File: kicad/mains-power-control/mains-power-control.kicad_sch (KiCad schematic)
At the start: 21 parts, among them J1 Conn_01x02_Socket, J2 Conn_01x03_Socket, J3 Conn_01x03_Pin, J4 Conn_01x06_Pin, J5 Conn_01x04_Pin, J6 Conn_01x02_Pin, U1 BP, U2 SeeeduinoXIAO, U3 MOC3020M, U5 H11AA1

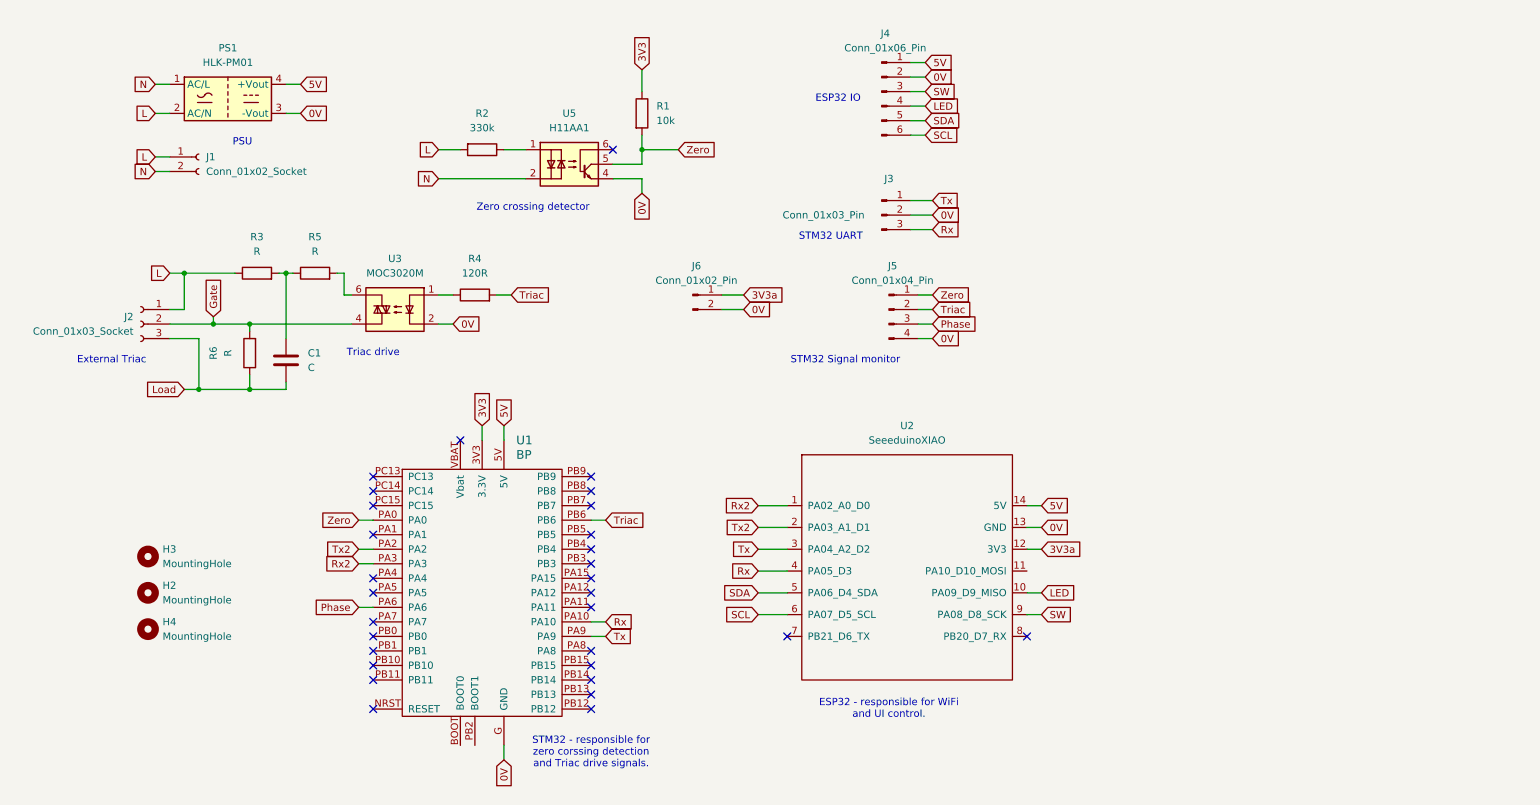
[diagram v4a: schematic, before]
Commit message: wip: adding fan driver and onewire to v 1.1 pcb
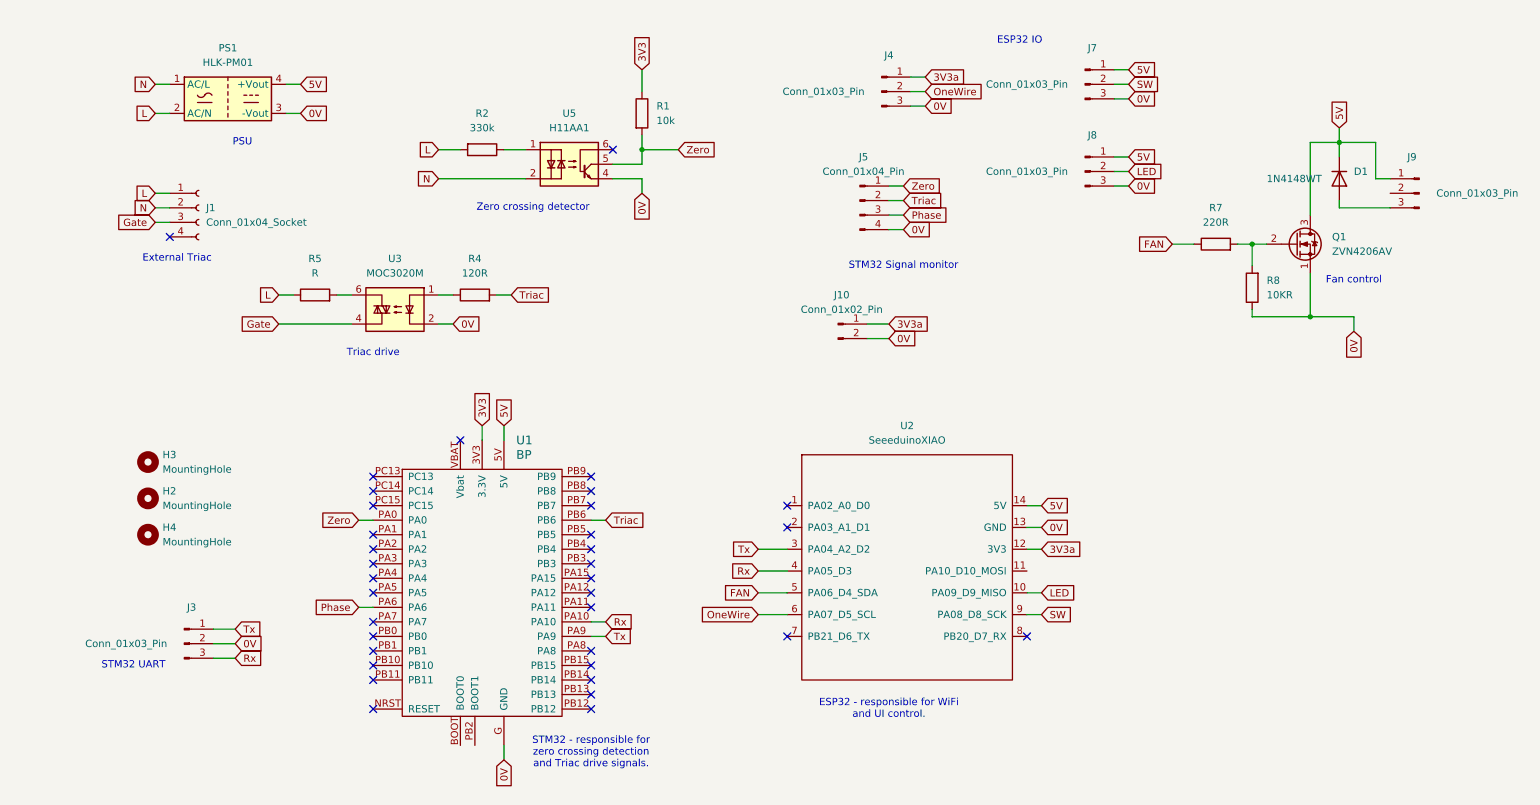
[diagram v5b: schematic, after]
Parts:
- removed C1: C, Capacitor_THT:C_Axial_L3.8mm_D2.6mm_P7.50mm_Horizontal, symbol Device:C
- removed J1: Conn_01x02_Socket, Connector_Phoenix_MC_HighVoltage:PhoenixContact_MCV_1,5_2-G-5.08_1x02_P5.08mm_Vertical, symbol Connector:Conn_01x02_Socket
- removed J2: Conn_01x03_Socket, Connector_PinHeader_2.54mm:PinHeader_1x03_P2.54mm_Vertical, symbol Connector:Conn_01x03_Socket
- removed J4: Conn_01x06_Pin, Connector_PinHeader_2.54mm:PinHeader_1x06_P2.54mm_Vertical, symbol Connector:Conn_01x06_Pin
- removed J6: Conn_01x02_Pin, Connector_PinHeader_2.54mm:PinHeader_1x02_P2.54mm_Vertical, symbol Connector:Conn_01x02_Pin
- removed R3, R6: R, Resistor_THT:R_Axial_DIN0207_L6.3mm_D2.5mm_P7.62mm_Horizontal, symbol Device:R
- added D1: 1N4148WT, Diode_THT:D_DO-41_SOD81_P7.62mm_Horizontal, symbol Diode:1N4148WT
- added J1: Conn_01x04_Socket, Connector_Phoenix_MC_HighVoltage:PhoenixContact_MCV_1,5_4-G-5.08_1x04_P5.08mm_Vertical, symbol Connector:Conn_01x04_Socket
- added J10: Conn_01x02_Pin, Connector_PinHeader_2.54mm:PinHeader_1x02_P2.54mm_Vertical, symbol Connector:Conn_01x02_Pin
- added J4, J7, J8, J9: Conn_01x03_Pin, Connector_PinHeader_2.54mm:PinHeader_1x03_P2.54mm_Vertical, symbol Connector:Conn_01x03_Pin
- added Q1: ZVN4206AV, Package_TO_SOT_THT:TO-92_Inline, symbol Transistor_FET:2N7000
- added R7: 220R, Resistor_THT:R_Axial_DIN0207_L6.3mm_D2.5mm_P7.62mm_Horizontal, symbol Device:R
- added R8: 10KR, Resistor_THT:R_Axial_DIN0207_L6.3mm_D2.5mm_P7.62mm_Horizontal, symbol Device:R
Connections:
- net 0V: now also J10.2 (Pin_2), J4.3 (Pin_3), J7.3 (Pin_3), J8.3 (Pin_3), Q1.1 (S), R8.1
- net 3V3a: now also J10.1 (Pin_1), J4.1 (Pin_1)
- net 5V: now also D1.1 (K), J7.1 (Pin_1), J8.1 (Pin_1), J9.1 (Pin_1), Q1.3 (D)
- net Gate: now also J1.3 (Pin_3)
- net L: now also R5.1, J1.1 (Pin_1)
- net LED: now also J8.2 (Pin_2)
- net N: now also J1.2 (Pin_2)
- net SW: now also J7.2 (Pin_2)
- net Rx2: no longer names the net of U1.PA3
- net Rx2: no longer U2.1 (PA02_A0_D0)
- net SCL renamed OneWire
- net OneWire: now also J4.2 (Pin_2)
- net SDA renamed FAN
- net FAN: now also R7.1
- net Tx2: no longer names the net of U1.PA2
- net Tx2: no longer U2.2 (PA03_A1_D1)
- new net: D1.2 (A), J9.3 (Pin_3)
- new net: Q1.2 (G), R7.2, R8.2
- no-connect marks 30 -> 35
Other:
- note added: "Fan control"
- note added: "STM32 - responsible for zero crossing detection and Triac drive signals."
- note removed: "STM32 - responsible for zero corssing detection and Triac drive signals."
- moved on the sheet: H2, H3, H4, J3, J5, R5

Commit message: wip: v1.1 pcb
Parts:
- removed J10: Conn_01x02_Pin, Connector_PinHeader_2.54mm:PinHeader_1x02_P2.54mm_Vertical, symbol Connector:Conn_01x02_Pin
- removed J5: Conn_01x04_Pin, Connector_PinHeader_2.54mm:PinHeader_1x04_P2.54mm_Vertical, symbol Connector:Conn_01x04_Pin
- added J2: Conn_01x06_Pin, Connector_PinHeader_2.54mm:PinHeader_1x06_P2.54mm_Vertical, symbol Connector:Conn_01x06_Pin
- D1: value 1N4148WT -> 1N4148
- R5: value R -> 150R
- R8: value 10KR -> 10K
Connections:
- net 0V: now also J2.5 (Pin_5)
- net 3V3a: now also J3.3 (Pin_3)
- net 5V: now also J3.1 (Pin_1), J9.2 (Pin_2); no longer J9.1 (Pin_1), Q1.3 (D)
- net Phase: now also J2.3 (Pin_3)
- net Rx: now also J2.6 (Pin_6); no longer J3.3 (Pin_3)
- net Triac: now also J2.2 (Pin_2)
- net Tx: now also J2.4 (Pin_4); no longer J3.1 (Pin_1)
- net Zero: now also J2.1 (Pin_1)
- net at D1.2 (A), J9.3 (Pin_3): now also Q1.3 (D)
- net fan_speed: now reaches U2.2 (PA03_A1_D1)
- net fan_speed: now also J9.1 (Pin_1)
- net SW renamed Switch
- no-connect marks 35 -> 34
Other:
- note added: "Aux Power"
- note added: "OneWire"
- note added: "Switch"
- note added: "WS2812 LEDs"
- note removed: "ESP32 IO"
- moved on the sheet: D1, J4, J7, J8, J9, Q1, R7, R8

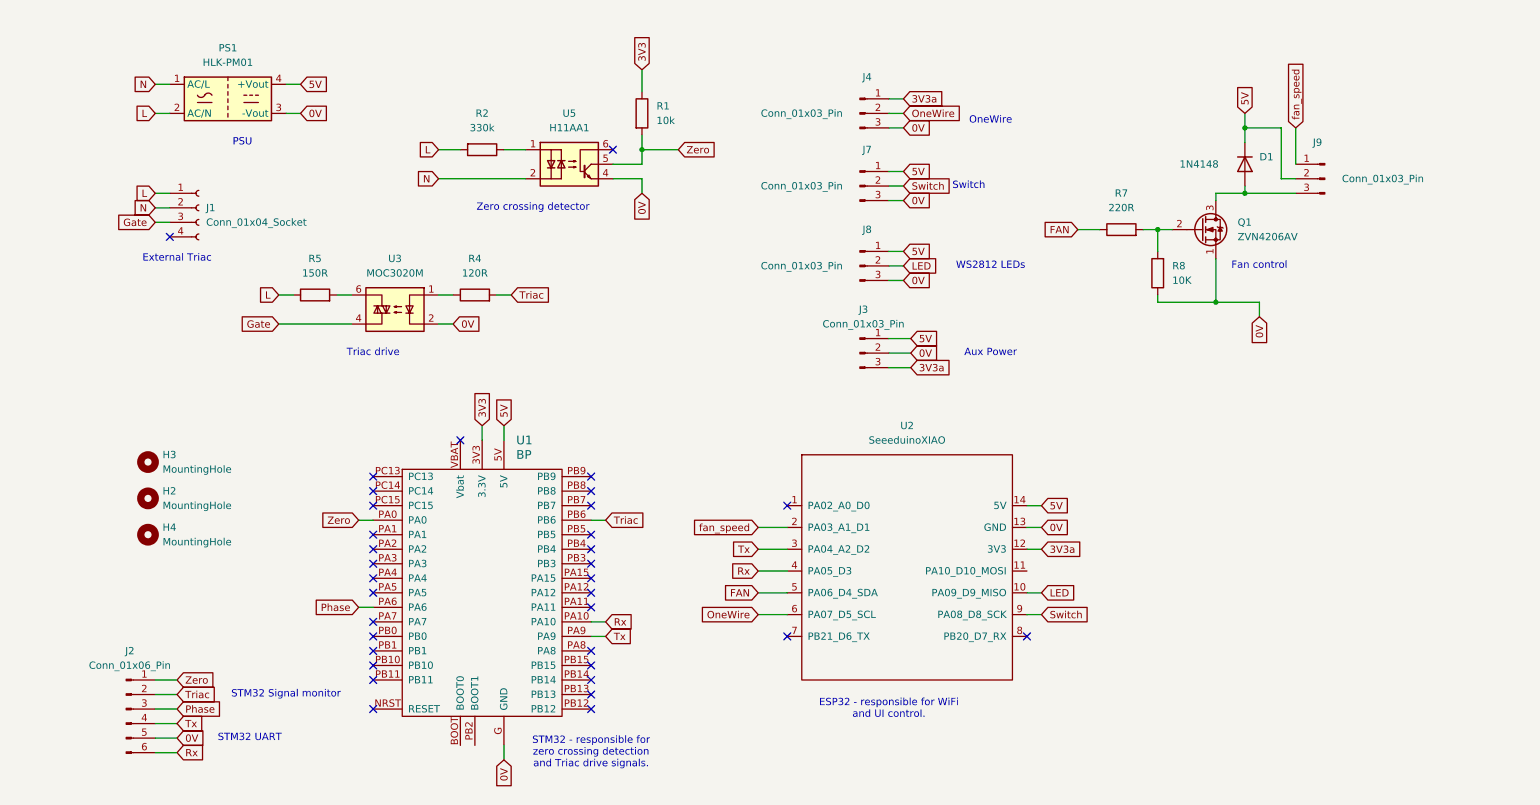
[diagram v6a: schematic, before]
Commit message: relay PCB to rotate the whole mounting - mains power now on one side
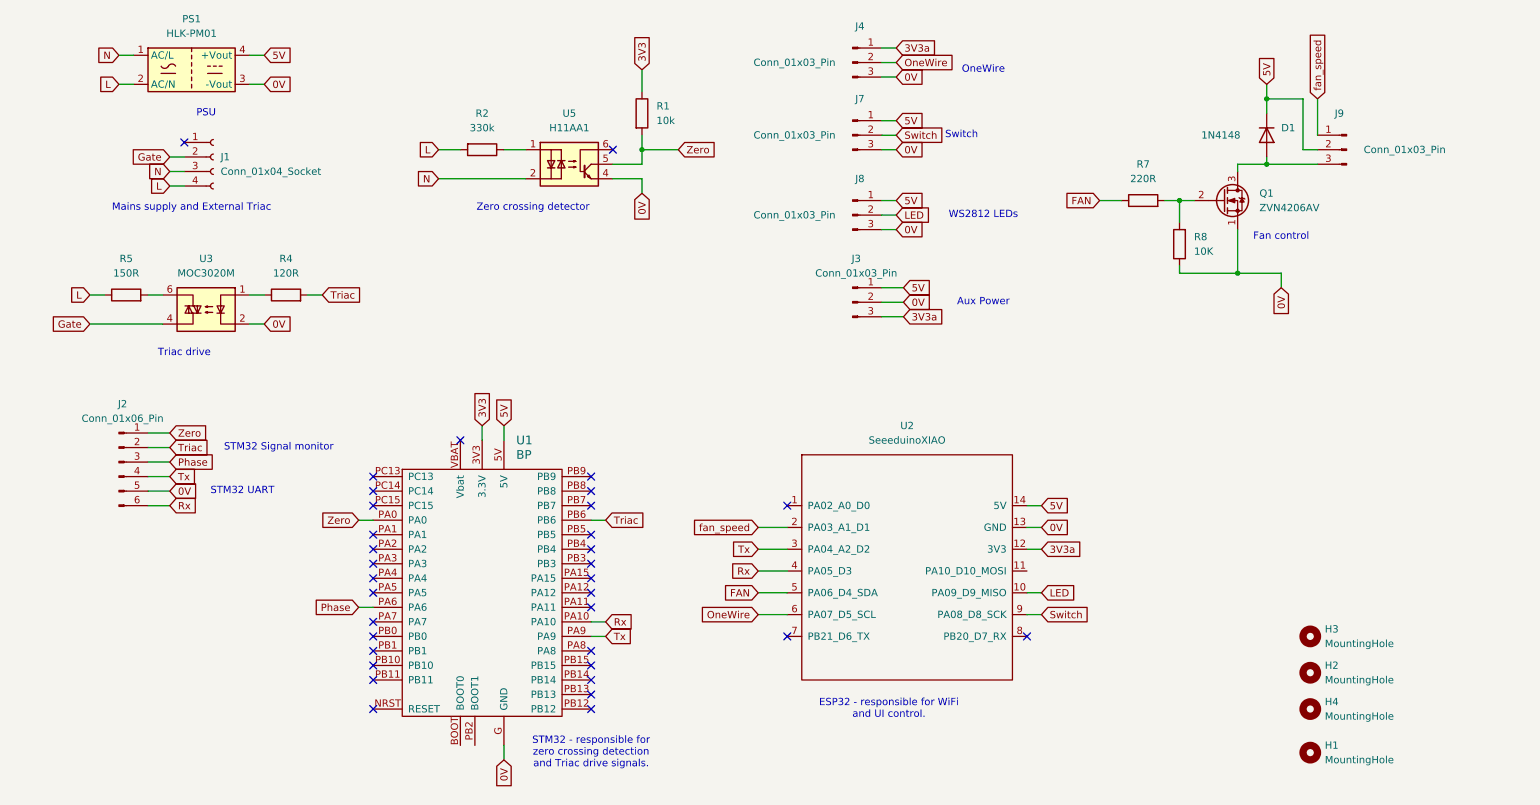
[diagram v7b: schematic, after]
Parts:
- added H1: MountingHole, MountingHole:MountingHole_3.2mm_M3, symbol Mechanical:MountingHole
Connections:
- net Gate: now also J1.2 (Pin_2); no longer J1.3 (Pin_3)
- net L: now also J1.4 (Pin_4); no longer J1.1 (Pin_1)
- net N: now also J1.3 (Pin_3); no longer J1.2 (Pin_2)
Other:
- note added: "Mains supply and External Triac"
- note removed: "External Triac"
- moved on the sheet: D1, H2, H3, H4, J1, J2, J3, J4, J7, J8, J9, PS1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

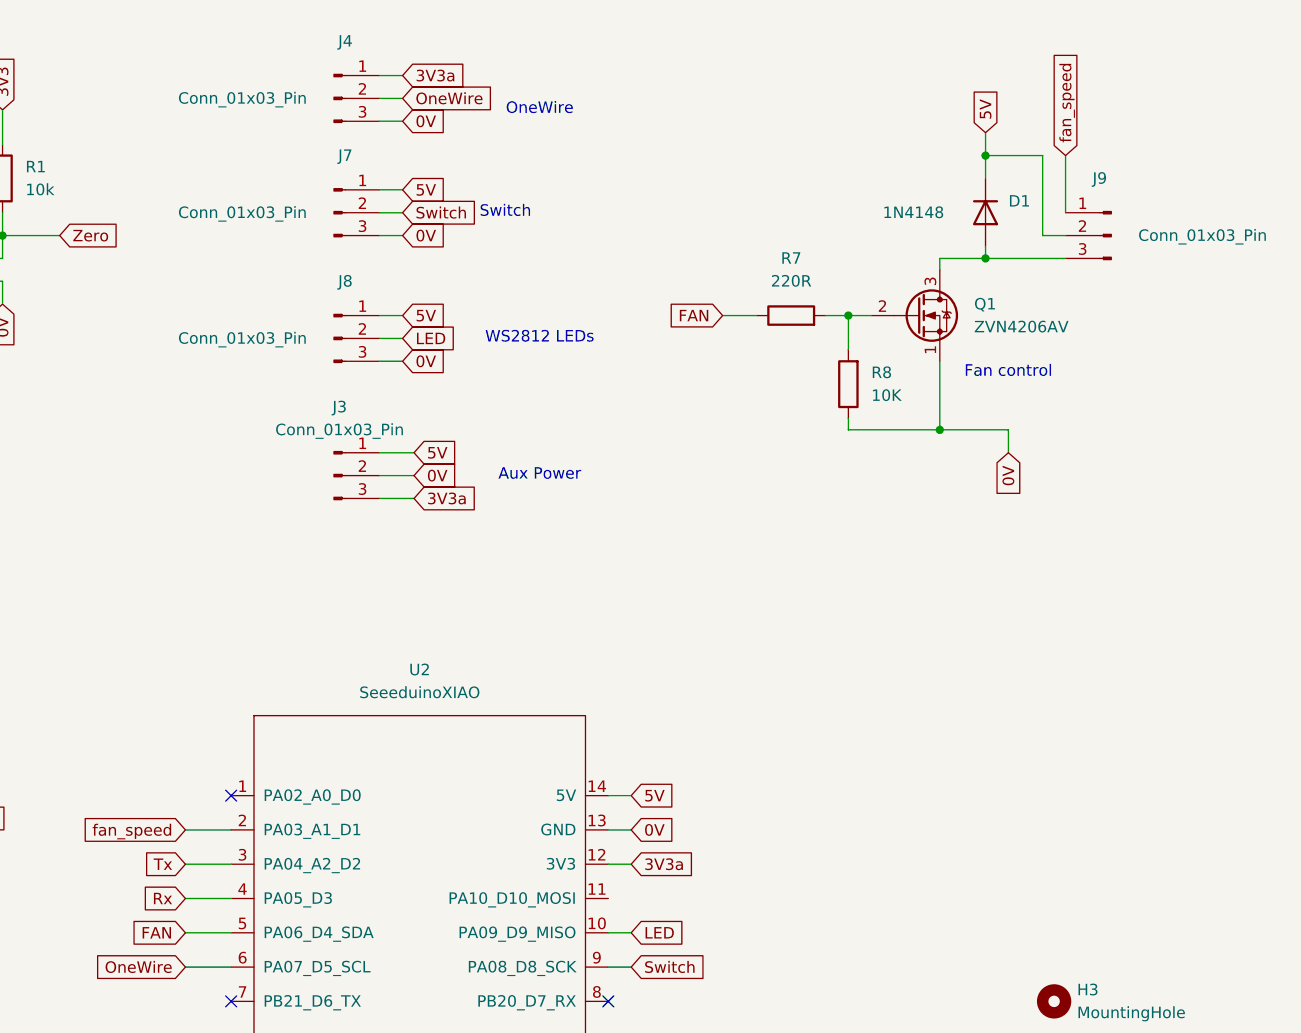
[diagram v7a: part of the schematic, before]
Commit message: put smarrt LEDs and hole for switch on pcb
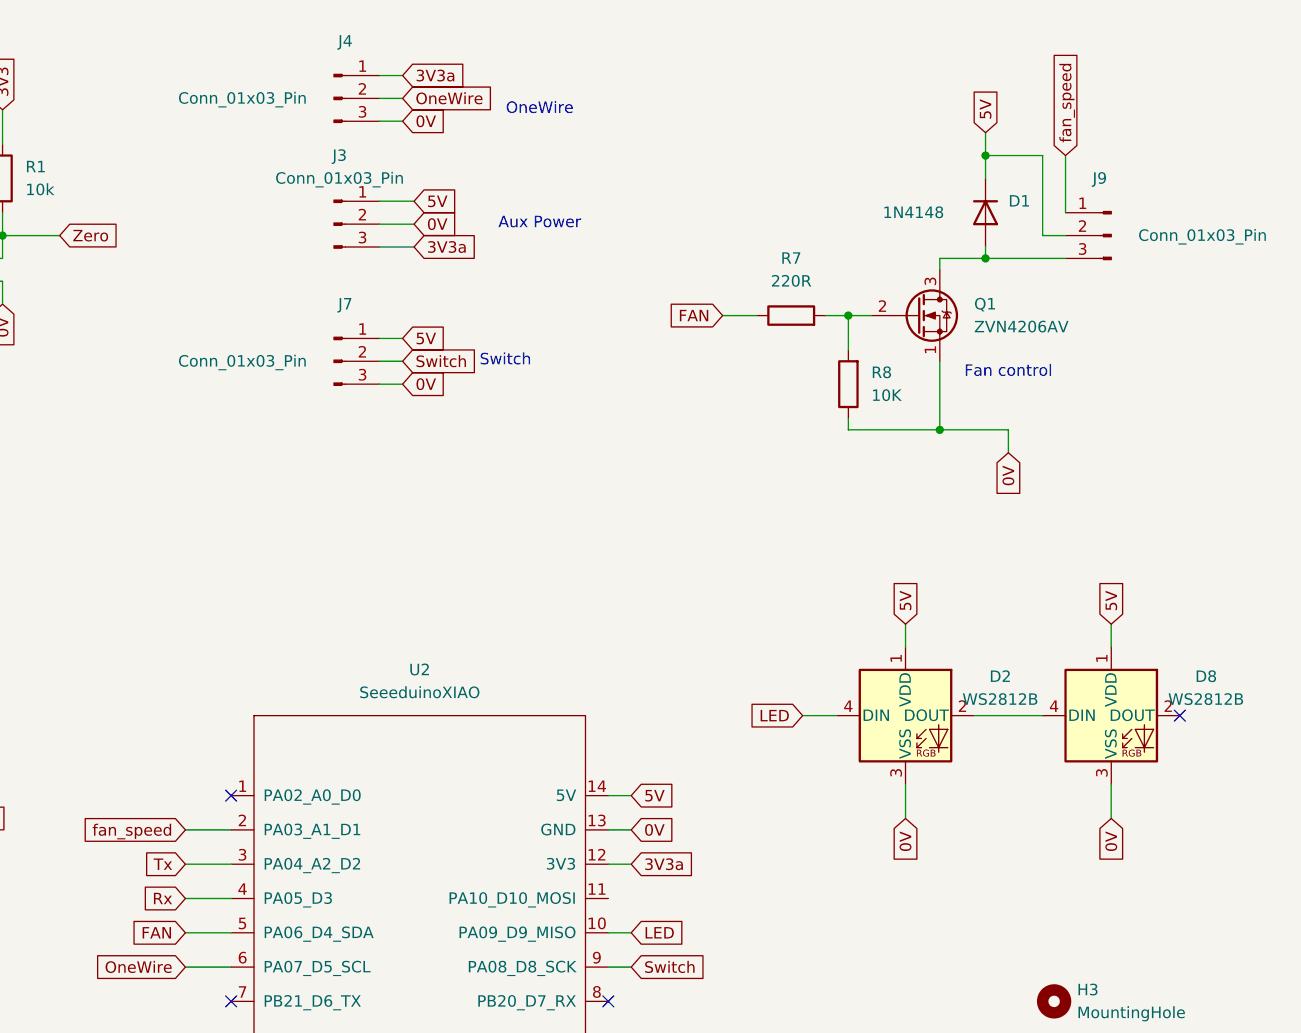
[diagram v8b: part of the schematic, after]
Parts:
- removed J8: Conn_01x03_Pin, Connector_PinHeader_2.54mm:PinHeader_1x03_P2.54mm_Vertical, symbol Connector:Conn_01x03_Pin
- added D2, D8: WS2812B, davelib:LED_D8-YF923, symbol LED:WS2812B
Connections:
- net 0V: now also D2.3 (VSS), D8.3 (VSS)
- net 5V: now also D2.1 (VDD), D8.1 (VDD)
- net LED: now also D2.4 (DIN)
- new net: D2.2 (DOUT), D8.4 (DIN)
- no-connect marks 34 -> 35
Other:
- note removed: "WS2812 LEDs"
- moved on the sheet: J3, J7
